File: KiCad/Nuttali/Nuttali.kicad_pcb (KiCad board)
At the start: 2 copper layers, 41 x 77.7 mm, 82 parts, among them J1 SWD, J2 B4B-XH-A, J3 Conn_01x03_Male, SW1 SW_DPST_x2, SW2 RND 210-00662, SW8 Rotary_Encoder, U1 STM32F411RETx, U2 PMW3389, U3 USBLC6-2P6, U4 AP131-15, U5 AP1117-15, U6 Button, U7 Button, U8 Scroll_button, U9 Button, Y1 16Mhz

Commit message: Missed saving things
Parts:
- moved U9 0.43 mm to (75.5, 91.2)
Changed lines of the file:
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@@
   )
   (module Nuttali:D2F-5 (layer F.Cu)
-    (at 75.25 91.6 90)
+    (at 75.5 91.25 90)
     (fp_text reference U9 (at 0 -7.5 90) (layer F.SilkS)
       (effects (font (size 1 1) (thickness 0.15)))

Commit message: Finnished the pcb
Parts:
- U5: footprint Package_TO_SOT_SMD:SOT-223-3_TabPin2 -> Package_TO_SOT_SMD:SOT-23
- moved TP6 175.0 mm to (51.0, 104.5)
- moved TP2 166.2 mm to (51.0, 102.5)
- moved TP4 164.1 mm to (51.0, 98.5)
- moved C11 161.8 mm to (63.2, 130.0)
- moved C23 161.0 mm to (56.0, 135.0), turned to 180 degrees
- moved C22 158.4 mm to (62.8, 135.0), turned to 90 degrees
- moved TP3 155.1 mm to (51.0, 100.5)
- moved C6 152.1 mm to (65.0, 118.2)
- moved TP5 150.0 mm to (51.0, 96.5)
- moved C10 149.1 mm to (63.2, 132.0), turned to 0 degrees
- moved J2 147.8 mm to (61.0, 139.5), turned to 90 degrees
- moved C25 146.2 mm to (59.2, 130.0), turned to 180 degrees
- moved R3 145.8 mm to (71.2, 93.0)
- moved C13 145.7 mm to (78.0, 135.5), turned to 270 degrees
- moved C5 145.6 mm to (80.5, 123.2), turned to 270 degrees
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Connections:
- C10 pad 2: VDDIO_3.3V -> +3V3
- C11 pad 1: VDDIO_3.3V -> +3V3
- C12 pad 1: VDDIO_3.3V -> +3V3
- C13 pad 1: VDDIO_3.3V -> +3V3
- C16 pad 1: VDDIO_3.3V -> +3V3
- C19 pad 1: VDDIO_3.3V -> +3V3
- C25 pad 1: VDDIO_3.3V -> +3V3
- C5 pad 1: VDDIO_3.3V -> +3V3
- C6 pad 2: VDDIO_3.3V -> +3V3
- C7 pad 2: VDDIO_3.3V -> +3V3
- C8 pad 2: VDDIO_3.3V -> +3V3
- C9 pad 2: VDDIO_3.3V -> +3V3
- J1 pad 6: VDDIO_3.3V -> +3V3
- J3 pad 1: VDDIO_3.3V -> +3V3
- R11 pad 1: WheelA -> +3V3
- R11 pad 2: Net-(R11-Pad2) -> WheelA
- R12 pad 2: Net-(R12-Pad2) -> +3V3
- R13 pad 1: Net-(R13-Pad1) -> +3V3
- R13 pad 2: WheelButton -> Net-(R13-Pad2)
- R15 pad 2: VDDIO_3.3V -> +3V3
- R2 pad 2: VDDIO_3.3V -> +3V3
- R6 pad 1: VDDIO_3.3V -> +3V3
- R7 pad 2: VDDIO_3.3V -> +3V3
- R8 pad 1: VDDIO_3.3V -> +3V3
- SW2 pad 1: VDDIO_3.3V -> +3V3
- SW8 pad A: Net-(R11-Pad2) -> WheelA
- SW8 pad B: Net-(R12-Pad2) -> WheelB
- U1 pad 1: VDDIO_3.3V -> +3V3
- U1 pad 13: VDDIO_3.3V -> +3V3
- U1 pad 15: R_LED -> B_LED
- U1 pad 17: B_LED -> R_LED
- U1 pad 19: VDDIO_3.3V -> +3V3
- U1 pad 23: WheelB -> WheelA
- U1 pad 24: WheelA -> WheelB
- U1 pad 32: VDDIO_3.3V -> +3V3
- U1 pad 48: VDDIO_3.3V -> +3V3
- U1 pad 64: VDDIO_3.3V -> +3V3
- U2 pad 5: VDDIO_3.3V -> +3V3
- U5 pad 2: VDDIO_3.3V -> +3V3
- U8 pad 2: VDDIO_3.3V -> WheelButton
- U8 pad 4: Net-(R13-Pad1) -> Net-(R13-Pad2)
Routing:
- net VDDIO_3.3V: track 364.3 -> 0.00 mm, vias 7 -> 0
- net +3V3: track 0.00 -> 234.9 mm, vias 0 -> 8
- net GND: track 265.0 -> 150.3 mm, vias 25 -> 14
- net +5V: track 118.5 -> 77.8 mm, vias 4 -> 2
- net Turbo_LED: track 11.3 -> 43.2 mm, vias 0 -> 2
- net RightB: track 98.1 -> 68.6 mm
- net B_LED: track 52.8 -> 25.2 mm
- net NCS: track 62.6 -> 36.3 mm, vias 4 -> 2
- net LeftB: track 80.6 -> 54.5 mm
- net +1V0: track 56.9 -> 35.6 mm, vias 0 -> 1
- net G_LED: track 49.6 -> 28.7 mm
- net MOSI: track 50.7 -> 31.0 mm
- net WheelA: track 55.3 -> 71.9 mm, vias 0 -> 1
- net R_LED: track 46.9 -> 30.4 mm
- net LED_1: track 2.32 -> 17.8 mm, vias 0 -> 1
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- added copper zone on B.Cu, net GND
- added copper zone on F.Cu, net GND
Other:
- board size 41 x 77.7 mm -> 41 x 80.8 mm

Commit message: Finnished design.
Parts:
- removed D4: LED, Nuttali:LED
- removed D5, D6, D7: LED_RGB, LED_SMD:LED_RGB_5050-6
- removed R19, R20, R21, R22, R23, R24: 220, Resistor_SMD:R_0805_2012Metric_Pad1.20x1.40mm_HandSolder
- added J4: Conn_01x02_Male, Connector_PinSocket_2.54mm:PinSocket_1x02_P2.54mm_Vertical, F.Cu at (59.1, 124.6)
- added J5: Conn_01x04_Male, Connector_PinSocket_2.54mm:PinSocket_1x04_P2.54mm_Vertical, F.Cu at (89.1, 113.8)
- added TP10: TestPoint, TestPoint:TestPoint_Pad_1.0x1.0mm, F.Cu at (60.7, 84.6)
- added TP11: TestPoint, TestPoint:TestPoint_Pad_1.0x1.0mm, F.Cu at (65.5, 92.2)
- added TP12: TestPoint, TestPoint:TestPoint_Pad_1.0x1.0mm, F.Cu at (65.5, 90.2)
- added TP13: TestPoint, TestPoint:TestPoint_Pad_1.0x1.0mm, F.Cu at (64.7, 87.6)
- added TP14: TestPoint, TestPoint:TestPoint_Pad_1.0x1.0mm, F.Cu at (62.7, 87.6)
- added TP15: TestPoint, TestPoint:TestPoint_Pad_1.0x1.0mm, F.Cu at (65.5, 95.6)
- moved R16 28.6 mm to (85.5, 121.4)
- moved R17 27.9 mm to (85.5, 119.4)
- moved R18 27.7 mm to (85.5, 117.4)
- moved TP6 17.6 mm to (67.3, 111.2)
- moved TP2 14.5 mm to (65.5, 103.6)
- moved TP3 14.5 mm to (65.5, 101.6)
- moved TP4 14.5 mm to (65.5, 99.6)
- moved TP5 14.5 mm to (65.5, 97.6)
- moved C28 1.57 mm to (59.7, 81.6), turned to 90 degrees
- moved C16 0.20 mm to (80.8, 102.1)
- moved C19 0.20 mm to (82.8, 102.1)
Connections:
- R16 pad 1: GND -> Net-(J5-Pad4)
- R16 pad 2: Net-(D5-Pad3) -> R_LED
- R17 pad 1: GND -> Net-(J5-Pad3)
- R17 pad 2: Net-(D5-Pad2) -> G_LED
- R18 pad 1: GND -> Net-(J5-Pad2)
- R18 pad 2: Net-(D5-Pad1) -> B_LED
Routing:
- net Turbo_LED: track 43.2 -> 8.54 mm, vias 2 -> 0
- net GND: track 150.3 -> 140.5 mm, vias 14 -> 12
- net R_LED: track 30.4 -> 22.8 mm
- net G_LED: track 28.7 -> 24.2 mm
- net +3V3: track 234.9 -> 238.3 mm, vias 8 -> 10
- net Turbo: track 49.7 -> 46.6 mm
- net Net-(J5-Pad2): track 0.00 -> 3.04 mm
- net B_LED: track 25.2 -> 22.4 mm
- net Net-(J5-Pad3): track 0.00 -> 2.82 mm
- net Net-(J5-Pad4): track 0.00 -> 2.61 mm
- net Net-(D6-Pad3): track 2.32 -> 0.00 mm
- net Net-(D6-Pad1): track 2.32 -> 0.00 mm
- net Net-(D6-Pad2): track 2.20 -> 0.00 mm
- net WheelA: track 71.9 -> 74.0 mm
- net LeftB: track 54.5 -> 56.1 mm
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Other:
- board text added: "A"
- board text added: "B"
- board text added: "LB"
- board text added: "MIOS"
- board text added: "MOSI"
- board text added: "Motion"
- board text added: "RB"
- board text added: "SCK"
- board text added: "Turbo"
- board text added: "WB"

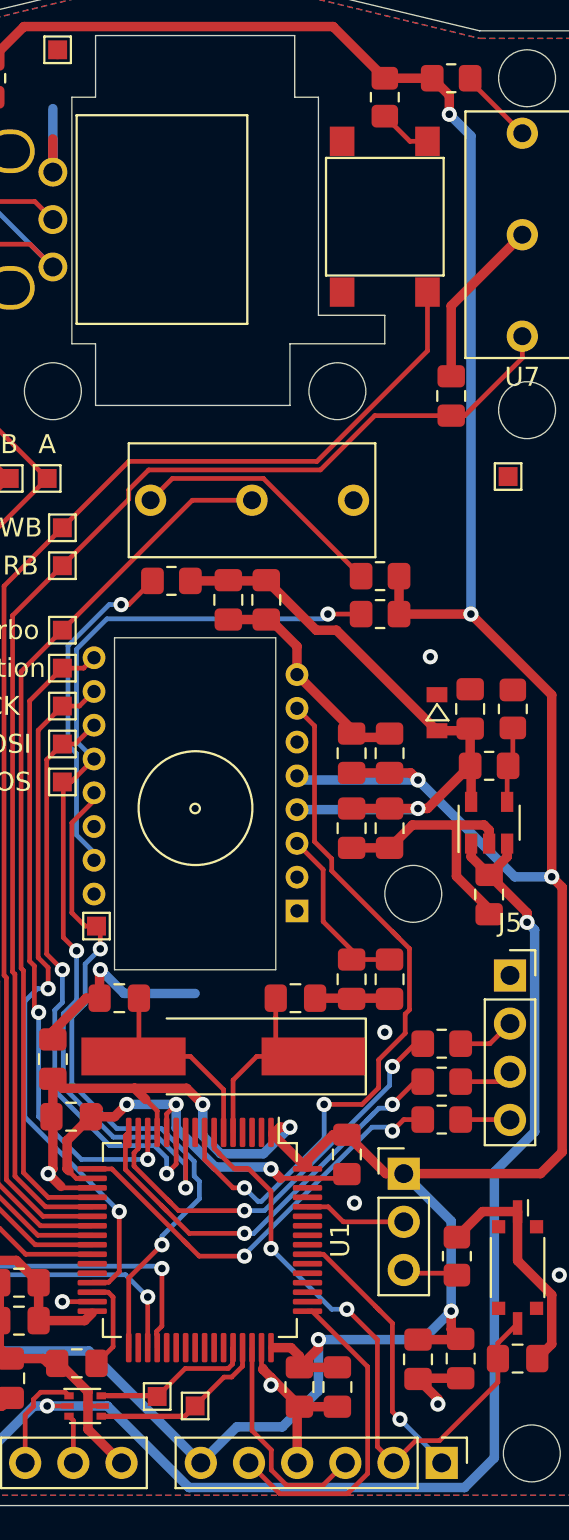
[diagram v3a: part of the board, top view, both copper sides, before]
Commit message: Changed routes on the scroll wheel button
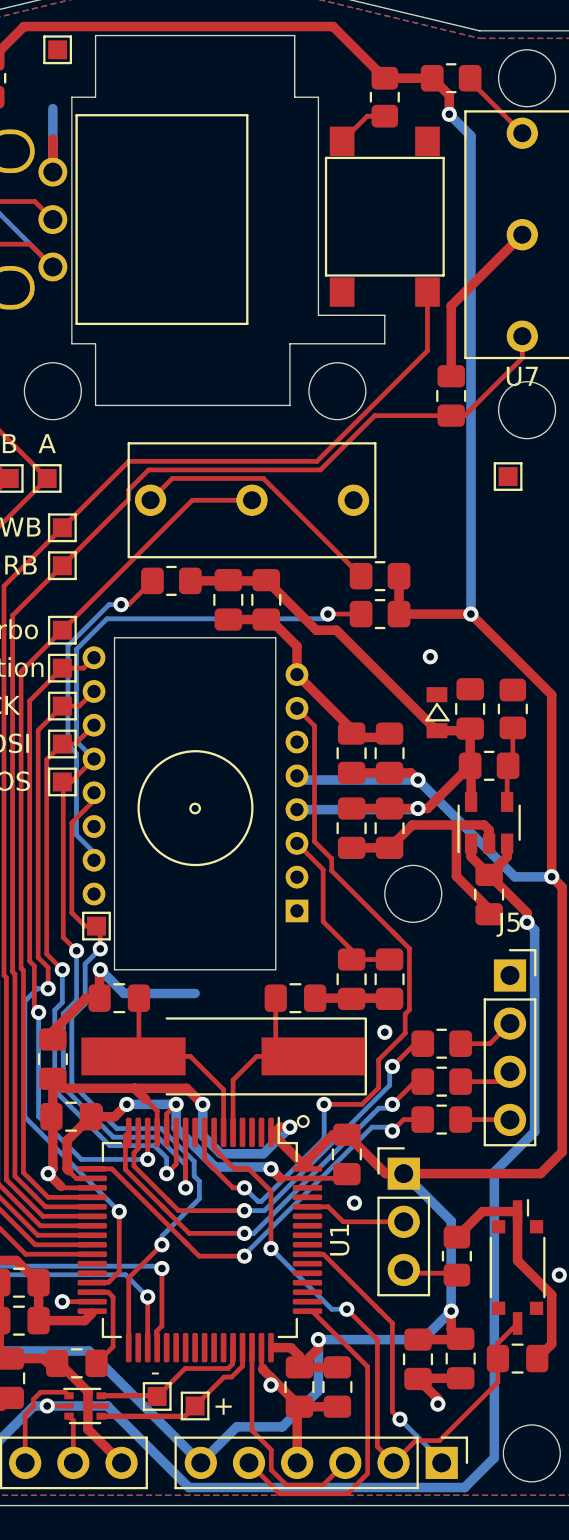
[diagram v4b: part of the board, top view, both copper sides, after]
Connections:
- U8 pad 3: Net-(U8-Pad3) -> Net-(R13-Pad2)
- U8 pad 4: Net-(R13-Pad2) -> Net-(U8-Pad4)
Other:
- board text added: "+"
- board text added: "-"

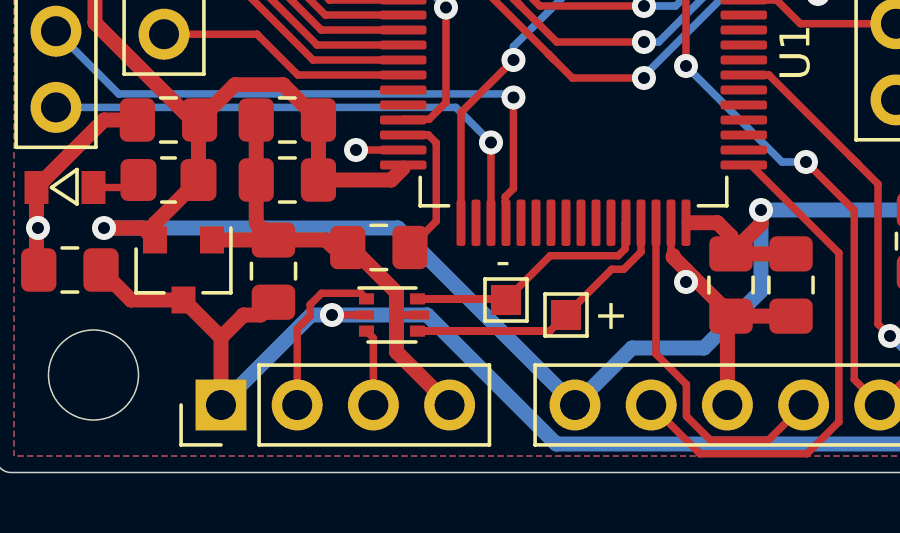
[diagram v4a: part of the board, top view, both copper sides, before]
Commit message: Chnages footprint of esd
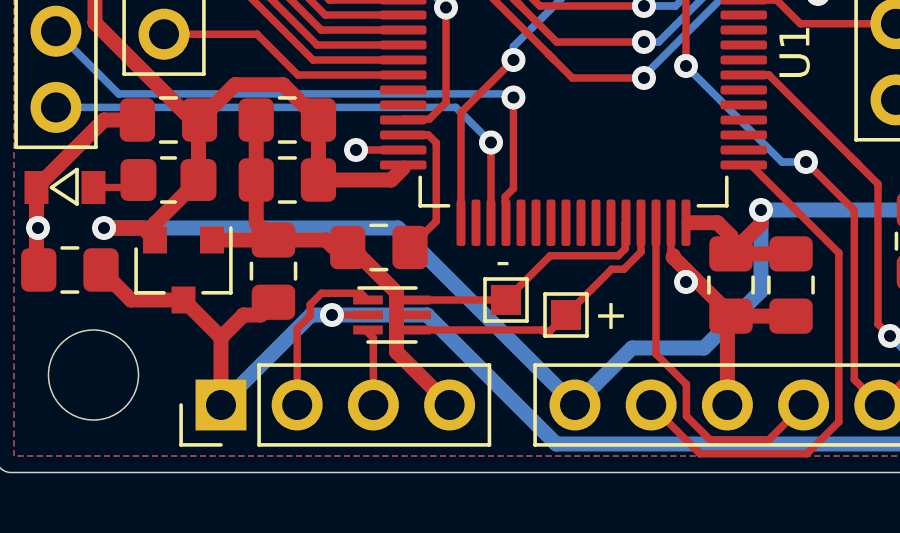
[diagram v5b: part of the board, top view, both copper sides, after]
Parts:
- U3: footprint Package_TO_SOT_SMD:SOT-666 -> PMW:SOT-666_ESD
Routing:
- net D+: track 13.4 -> 9.58 mm
- net D-: track 11.1 -> 8.61 mm
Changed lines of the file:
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@@
     (thickness 1.6)
     (drawings 62)
-    (tracks 631)
+    (tracks 630)
     (zones 0)
     (modules 80)
@@
     (uvia_drill 0.1)
   )
+  (module PMW:SOT-666_ESD (layer F.Cu)
+    (at 66.7 136.5)
+    (descr SOT666)
+    (tags SOT-666)
+    (attr smd)
+    (fp_text reference U3 (at 0 -1.75) (layer F.Fab)
+      (effects (font (size 1 1) (thickness 0.15)))
+    )
+    (fp_text value USBLC6-2P6 (at 0 1.75 180) (layer F.Fab)
+      (effects (font (size 1 1) (thickness 0.15)))
+    )
+    (fp_text user %R (at 0 0 90) (layer F.Fab)
+      (effects (font (size 0.5 0.5) (thickness 0.075)))
+    )
+    (fp_line (start 1.5 1.1) (end 1.5 -1.1) (layer F.CrtYd) (width 0.05))
+    (fp_line (start -1.5 -1.1) (end -1.5 1.1) (layer F.CrtYd) (width 0.05))
+    (fp_line (start 0.65 0.85) (end -0.65 0.85) (layer F.Fab) (width 0.1))
+    (fp_line (start 0.65 -0.85) (end 0.65 0.85) (layer F.Fab) (width 0.1))
+    (fp_line (start -1.5 1.1) (end 1.5 1.1) (layer F.CrtYd) (width 0.05))
+    (fp_line (start -0.65 -0.53) (end -0.65 0.85) (layer F.Fab) (width 0.1))
+    (fp_line (start 0.65 -0.85) (end -0.33 -0.85) (layer F.Fab) (width 0.1))
+    (fp_line (start -1.5 -1.1) (end 1.5 -1.1) (layer F.CrtYd) (width 0.05))
+    (fp_line (start -0.8 0.9) (end 0.8 0.9) (layer F.SilkS) (width 0.12))
+    (fp_line (start 0.8 -0.9) (end -1.1 -0.9) (layer F.SilkS) (width 0.12))
+    (fp_line (start -0.65 -0.53) (end -0.33 -0.85) (layer F.Fab) (width 0.1))
+    (pad 6 smd rect (at 0.8 -0.5 90) (size 0.3 0.99) (layers F.Cu F.Paste F.Mask)
+      (net 26 D-))
+    (pad 4 smd rect (at 0.8 0.5 90) (size 0.3 0.99) (layers F.Cu F.Paste F.Mask)
+      (net 27 D+))
+    (pad 2 smd rect (at -0.8 0) (size 0.99 0.3) (layers F.Cu F.Paste F.Mask)
+      (net 6 +5V))
+    (pad 5 smd rect (at 0.8 0 90) (size 0.3 0.99) (layers F.Cu F.Paste F.Mask)
+      (net 1 GND))
+    (pad 3 smd rect (at -0.8 0.5 90) (size 0.3 0.99) (layers F.Cu F.Paste F.Mask)
+      (net 14 "Net-(J2-Pad3)"))
+    (pad 1 smd rect (at -0.8 -0.5 90) (size 0.3 0.99) (layers F.Cu F.Paste F.Mask)
+      (net 13 "Net-(J2-Pad2)"))
+    (model ${KISYS3DMOD}/Package_TO_SOT_SMD.3dshapes/SOT-666.wrl
+      (at (xyz 0 0 0))
+      (scale (xyz 1 1 1))
+      (rotate (xyz 0 0 0))
+    )
+  )
   (module Package_QFP:LQFP-64_10x10mm_P0.5mm (layer F.Cu)
     (at 72.75 127.75 270)
@@
       (net 1 GND))
   )
-  (module Package_TO_SOT_SMD:SOT-666 (layer F.Cu)
-    (at 66.7 136.5)
-    (descr SOT666)
-    (tags SOT-666)
-    (attr smd)
-    (fp_text reference U3 (at 0 -1.75) (layer F.Fab)
-      (effects (font (size 1 1) (thickness 0.15)))
-    )
-    (fp_text value USBLC6-2P6 (at 0 1.75 180) (layer F.Fab)
-      (effects (font (size 1 1) (thickness 0.15)))
-    )
-    (fp_line (start 1.5 1.1) (end 1.5 -1.1) (layer F.CrtYd) (width 0.05))
-    (fp_line (start -1.5 -1.1) (end -1.5 1.1) (layer F.CrtYd) (width 0.05))
-    (fp_line (start 0.65 0.85) (end -0.65 0.85) (layer F.Fab) (width 0.1))
-    (fp_line (start 0.65 -0.85) (end 0.65 0.85) (layer F.Fab) (width 0.1))
-    (fp_line (start -1.5 1.1) (end 1.5 1.1) (layer F.CrtYd) (width 0.05))
-    (fp_line (start -0.65 -0.53) (end -0.65 0.85) (layer F.Fab) (width 0.1))
-    (fp_line (start 0.65 -0.85) (end -0.33 -0.85) (layer F.Fab) (width 0.1))
-    (fp_line (start -1.5 -1.1) (end 1.5 -1.1) (layer F.CrtYd) (width 0.05))
-    (fp_line (start -0.8 0.9) (end 0.8 0.9) (layer F.SilkS) (width 0.12))
-    (fp_line (start 0.8 -0.9) (end -1.1 -0.9) (layer F.SilkS) (width 0.12))
-    (fp_line (start -0.65 -0.53) (end -0.33 -0.85) (layer F.Fab) (width 0.1))
-    (fp_text user %R (at 0 0 90) (layer F.Fab)
-      (effects (font (size 0.5 0.5) (thickness 0.075)))
-    )
-    (pad 1 smd rect (at -0.85 -0.5375) (size 0.5 0.375) (layers F.Cu F.Paste F.Mask)
-      (net 13 "Net-(J2-Pad2)"))
-    (pad 3 smd rect (at -0.85 0.5375) (size 0.5 0.375) (layers F.Cu F.Paste F.Mask)
-      (net 14 "Net-(J2-Pad3)"))
-    (pad 5 smd rect (at 0.925 0) (size 0.65 0.3) (layers F.Cu F.Paste F.Mask)
-      (net 1 GND))
-    (pad 2 smd rect (at -0.925 0) (size 0.65 0.3) (layers F.Cu F.Paste F.Mask)
-      (net 6 +5V))
-    (pad 4 smd rect (at 0.85 0.5375) (size 0.5 0.375) (layers F.Cu F.Paste F.Mask)
-      (net 27 D+))
-    (pad 6 smd rect (at 0.85 -0.5375) (size 0.5 0.375) (layers F.Cu F.Paste F.Mask)
-      (net 26 D-))
-    (model ${KISYS3DMOD}/Package_TO_SOT_SMD.3dshapes/SOT-666.wrl
-      (at (xyz 0 0 0))
-      (scale (xyz 1 1 1))
-      (rotate (xyz 0 0 0))
-    )
-  )
   (module Package_TO_SOT_SMD:SOT-23-5 (layer F.Cu)
     (at 88 105.75 90)
@@
   (segment (start 70.75 127.55) (end 70.75 128) (width 0.25) (layer B.Cu) (net 25))
   (segment (start 72.725001 125.574999) (end 70.75 127.55) (width 0.25) (layer B.Cu) (net 25))
-  (segment (start 67.85 135.9625) (end 70.4625 135.9625) (width 0.25) (layer F.Cu) (net 26))
   (segment (start 74.47501 133.44999) (end 74.5 133.425) (width 0.25) (layer F.Cu) (net 26))
   (segment (start 74.47501 134.290692) (end 74.47501 133.44999) (width 0.25) (layer F.Cu) (net 26))
@@
   (segment (start 70.5 136) (end 71.97499 134.52501) (width 0.25) (layer F.Cu) (net 26))
   (segment (start 70.4625 135.9625) (end 70.5 136) (width 0.25) (layer F.Cu) (net 26))
-  (segment (start 67.55 135.9625) (end 70.4625 135.9625) (width 0.25) (layer F.Cu) (net 26))
+  (segment (start 67.5 136) (end 70.5 136) (width 0.25) (layer F.Cu) (net 26))
   (segment (start 71.9625 137.0375) (end 72.5 136.5) (width 0.25) (layer F.Cu) (net 27))
   (segment (start 74.427093 134.975019) (end 75 134.402112) (width 0.25) (layer F.Cu) (net 27))
@@
   (segment (start 72.5 136.5) (end 74.02498 134.97502) (width 0.25) (layer F.Cu) (net 27))
   (segment (start 71.7375 137.0375) (end 71.9625 137.0375) (width 0.25) (layer F.Cu) (net 27))
-  (segment (start 67.55 137.0375) (end 71.7375 137.0375) (width 0.25) (layer F.Cu) (net 27))
-  (segment (start 67.85 137.0375) (end 71.7375 137.0375) (width 0.25) (layer F.Cu) (net 27))
+  (segment (start 71.7 137) (end 71.7375 137.0375) (width 0.25) (layer F.Cu) (net 27))
+  (segment (start 67.5 137) (end 71.7 137) (width 0.25) (layer F.Cu) (net 27))
   (via (at 75.1 125) (size 0.8) (drill 0.4) (layers F.Cu B.Cu) (net 31))
   (via (at 79.3 120.6) (size 0.8) (drill 0.4) (layers F.Cu B.Cu) (net 31))

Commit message: Last push befor ordering
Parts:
- SW1: footprint Button_Switch_SMD:SW_DIP_SPSTx01_Slide_Copal_CVS-01xB_W5.9mm_P1mm -> Button_Switch_SMD:SW_SPST_B3U-1000P
- U3: footprint PMW:SOT-666_ESD -> Package_TO_SOT_SMD:SOT-666
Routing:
- net GND: track 140.5 -> 135.7 mm
- net NRST: track 33.7 -> 35.0 mm
- net WheelA: track 74.0 -> 74.7 mm

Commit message: PCB done
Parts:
- U3: footprint Package_TO_SOT_SMD:SOT-666 -> PMW:SOT-666_ESD
- moved R16 0.10 mm to (85.4, 121.4)
- moved R17 0.10 mm to (85.4, 119.4)
- moved R18 0.10 mm to (85.4, 117.4)
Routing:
- net GND: track 135.7 -> 148.9 mm, vias 12 -> 14
- net +5V: track 78.1 -> 80.6 mm
